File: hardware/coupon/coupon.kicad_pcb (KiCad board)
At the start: 4 copper layers, 100 x 80 mm, 78 parts, among them SW1 tactile

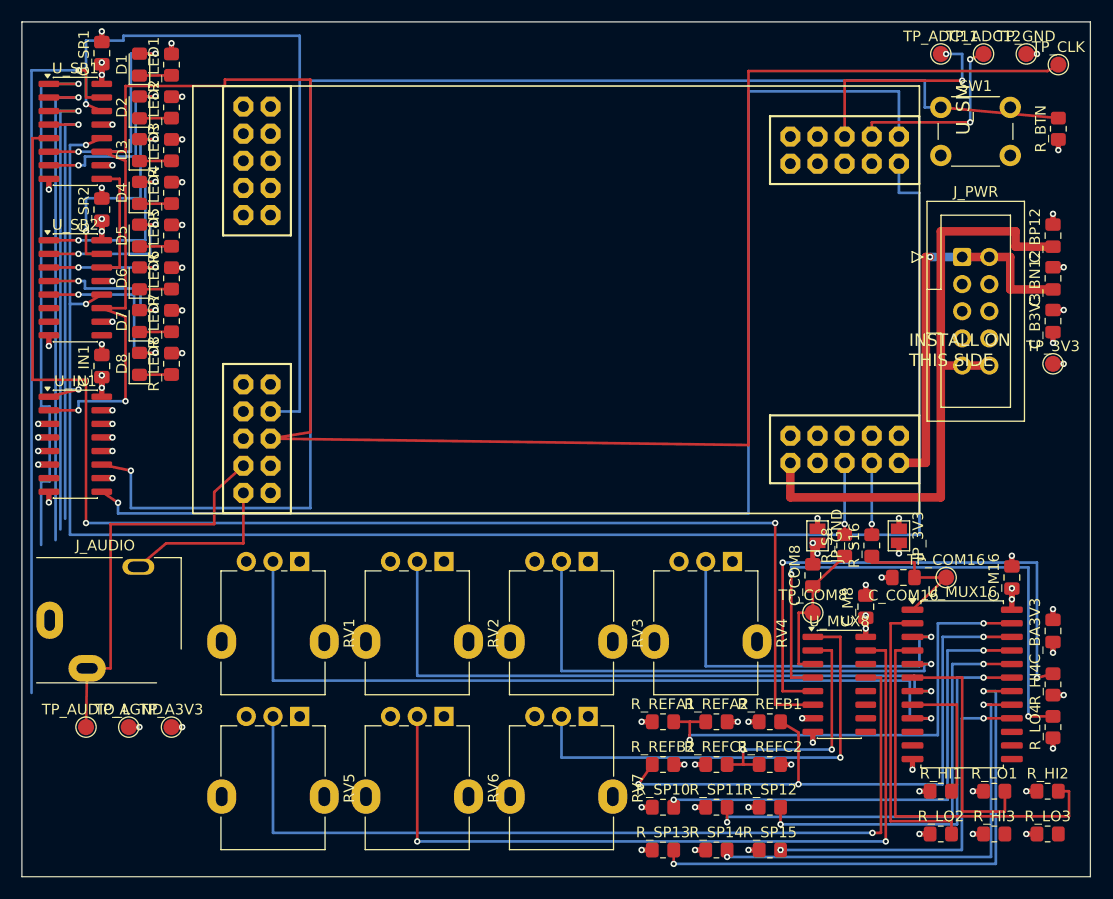
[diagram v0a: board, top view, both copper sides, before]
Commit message: hw(coupon): the tie comes to the mux, and the latch leaves the moat
Two controller rulings, both taken.

placement.py is data, so R_LO3 moved: (96, 76) -> (77.4, 69.6), 1.35 mm below
the 8:1's south edge and 6.3 mm from the pin it ties instead of 22. MUX8_CH3
is now a two-corner F.Cu drop through the package's own interior with no via,
and MUX8_CH1 -- unroutable last pass -- reaches R_HI3 down the strip between
the packages and along the board's southern edge, also without a via. Every
gate that depends on placement re-ran green, the stitcher re-derived its vias
around the moved part by itself, and the ratsnest went 11 -> 8.

R_HI3 stayed, and R_HI4/R_LO4 stayed, and both are decisions rather than
omissions -- the report has the arithmetic. The short version: the strip
between the two SOICs is 1.725 mm and carries four nets in four 0.45 mm
lanes, so a tie parked in it strands two of them; and the only slot within
5 mm of the 8:1's west-column pins is also the only F.Cu approach to its
enable, where a tie's stitching via lands 0.005 mm off the enable's lane.

SR_LATCH no longer runs the width of the board inside the plane gap. It sits
at y 47.4 now, inside the digital plane, which needed the two sense-drop vias
moved from y 47.0 to 46.2 -- at 47.0 there was no lane at all between
JP_GND's stitching via and the moat. Five moat crossings remain, all
perpendicular, none parallel to the gap.

Eight pairs are still open, all of them the address bus and the 16:1's enable
landing at the muxes. The corridor between the west edge and the muxes has
exactly one free 0.45 mm lane left and five nets want it; freeing the two
lanes MUX8_CH5/CH7 hold means bringing their ties to the package too, which
is a placement pass of its own.

Co-Authored-By: HAL 9000 <293417720+bea-ton-k@users.noreply.github.com>
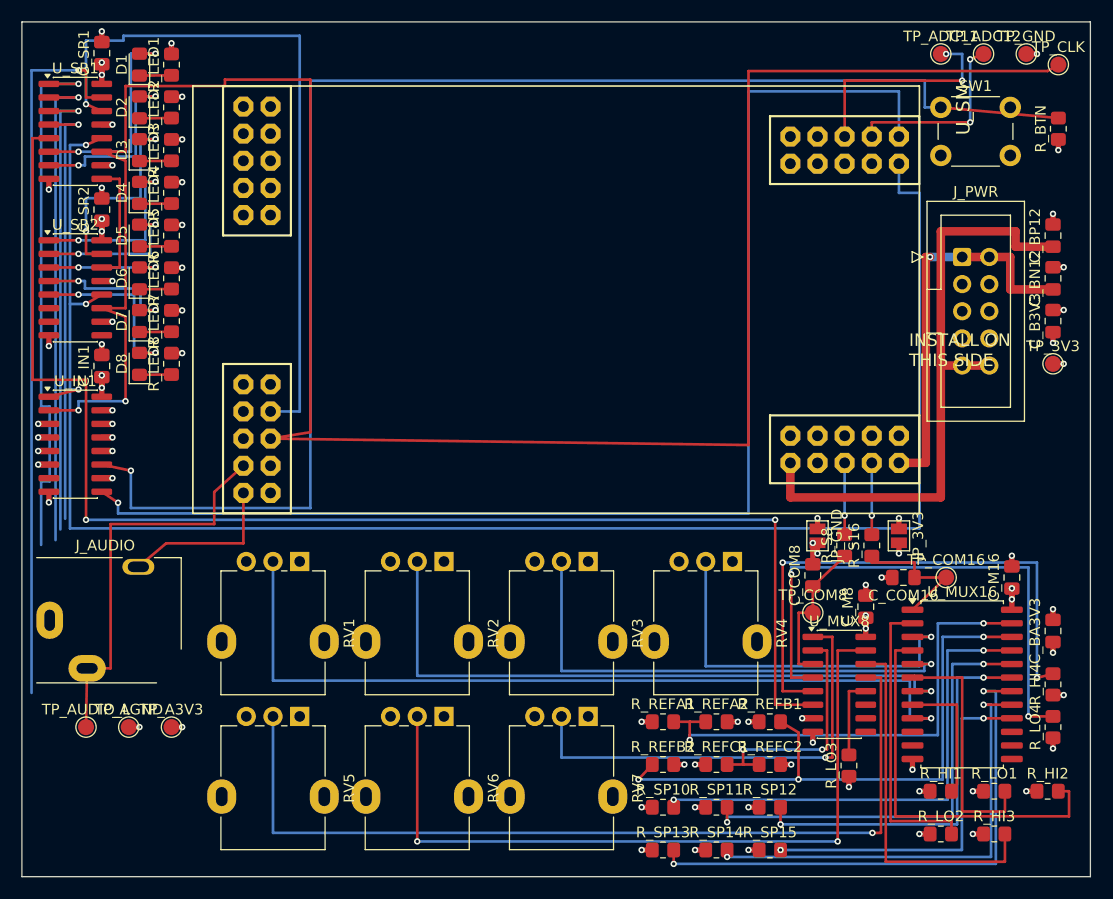
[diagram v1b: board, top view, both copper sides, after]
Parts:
- moved R_LO3 19.7 mm to (77.4, 69.6), turned to 90 degrees
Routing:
- net MUX8_CH1: track 0.00 -> 34.1 mm
- net MUX8_CH3: track 0.00 -> 7.54 mm
- net MUX8_CH2: track 75.3 -> 71.5 mm
- net MUX8_CH4: track 43.8 -> 42.3 mm
- net MUX16_CH9: track 57.8 -> 56.6 mm
- net SR_LATCH: track 162.6 -> 161.4 mm
- net MUX8_CH6: track 23.7 -> 22.8 mm

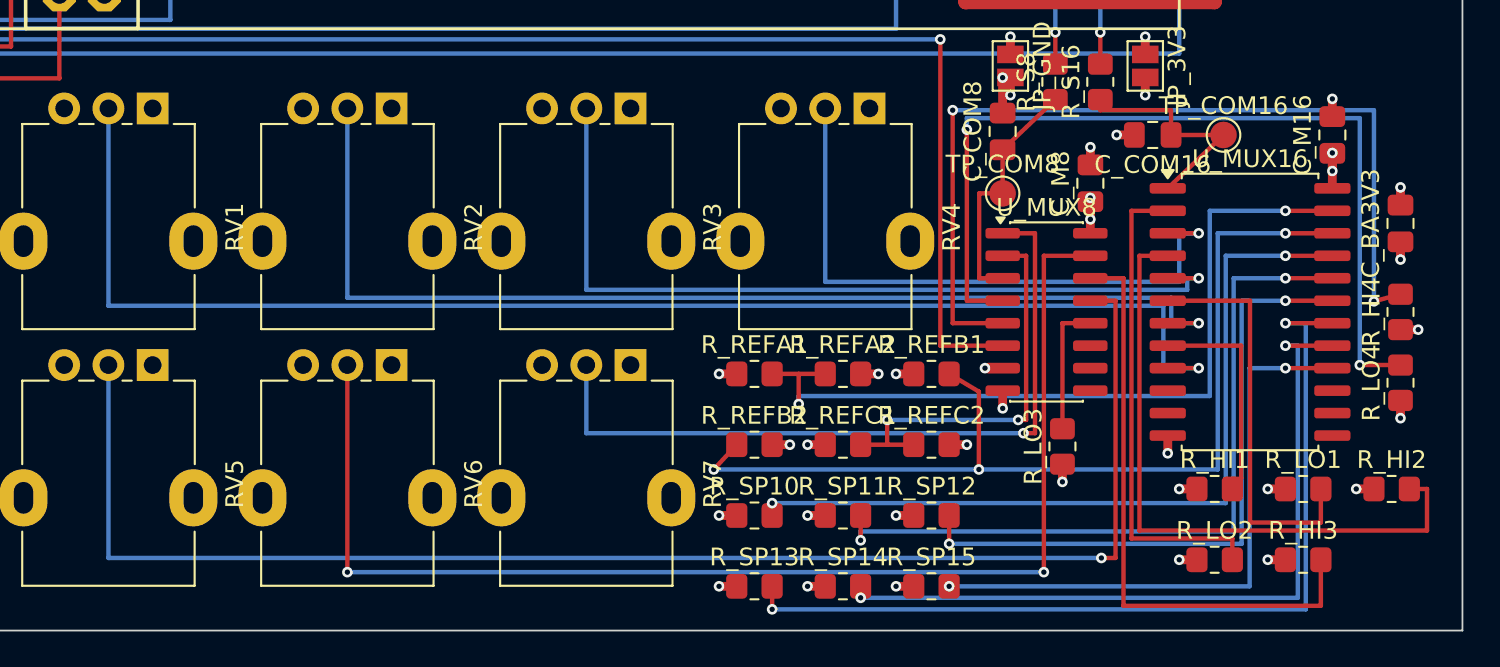
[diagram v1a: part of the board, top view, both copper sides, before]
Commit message: hw(coupon): WIP -- the interior takes the whole column, the strip empties
Placement pass 2, paused mid-flight. Steps 1-5 green; step 6 red with 3
tracks_crossing, all one cause -- MUX16_CH7's F.Cu vertical at x 86.0 cuts
the three stubs leaving the 16:1's west pad column at x 83.35 (CH5 at y
58.825, CH3 at 61.365, CH1 at 63.905). Step 7 red at 8 pairs: the address
bus and the 16:1's enable, unchanged.

What moved: R_LO3 to (78.4, 69.6) so the 8:1's interior can hold six 0.45 mm
lanes instead of five; MUX16_CH5 and CH7 out of the strip into the tie-row
gap; MUX8_CH0, CH1 and CH2 out of the strip into that interior. The strip
between the two packages is now empty, which is the point: MUX_A0 and MUX_A1
have to bridge the 8:1's east column and the 16:1's west column at y 63.905
and 65.175, and any full-height descent in that 2.375 mm strip cuts the
bridge.

R_LO4 went to the 8:1's west flank and came back. The finding is measured,
not assumed: its pads span x 70.9..72.3, which is where MUX8_CH5's only west
exit runs, and the corridor left between those pads and MUX8_COM's fixed
vertical at x 72.7 is 0.4 mm against the 0.65 mm a 0.25 mm track needs. The
interior cannot absorb CH5 either -- its six lanes are the 8:1's whole right
column plus the two left-column channels that MUX8_COM blocks from leaving
west.

Co-Authored-By: HAL 9000 <293417720+bea-ton-k@users.noreply.github.com>
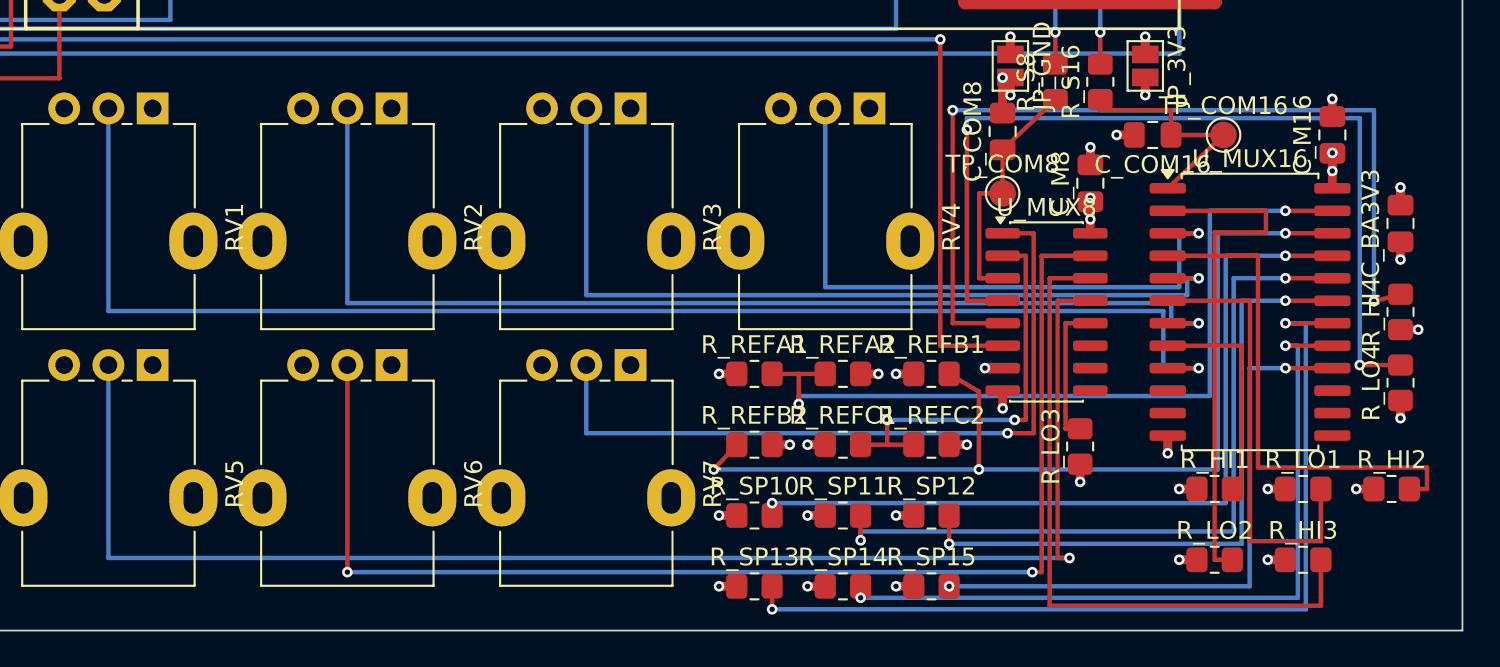
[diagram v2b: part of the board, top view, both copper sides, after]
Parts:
- moved R_LO3 1.00 mm to (78.4, 69.6)
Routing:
- net MUX16_CH5: track 36.7 -> 28.8 mm
- net MUX8_CH1: track 34.1 -> 38.7 mm
- net MUX16_CH3: track 23.1 -> 25.2 mm
- net MUX16_CH7: track 27.5 -> 29.2 mm
- net MUX8_CH0: track 83.8 -> 82.3 mm
- net MUX8_CH3: track 7.54 -> 8.19 mm
- net MUX16_CH6: track 35.4 -> 36.0 mm
- net MUX16_CH4: track 47.3 -> 47.9 mm

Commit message: hw(coupon): the SMD pads were never walls, and the last net lands
The pause left one crossing and eight unconnected pairs, and the intended
fix -- a descent east of the west-column stubs -- turns out not to exist:
the only lane there sits west of CH5's stub end, and any descent that does
clear it is then crossed by CH3's own leg to R_LO1. CH7 goes west into the
strip instead and comes back between the tie rows. No via, no crossing.

The address bus moved on one measurement: every mux, cap, resistor and
test-point pad on this board is SMD, so it blocks F.Cu only. B.Cu runs
under both SOICs, under both tie rows and under every 0805, and what
actually walls the analog half off is Task 3's stitching, the pots' and the
jack's through-holes, and this task's own earlier lanes. Three corridors
fall out of that: the y-62 band under the 8:1, the F.Cu band between the
upper pots' pins and their lugs, and the single lane that threads C_M8's
and C_M16's vias at y 54.75. A0/A1/A2 take the first, A3 and EN16 the
second and third, and all five reach the 16:1's east column through the
2.1 mm pocket east of the package -- the interior is closed by eight via
stubs and six descents, enumerated, not assumed.

CH8 and MUX8_CH1 gave up a lane each so the strip bridges and the south
runs have somewhere to be. Nothing in placement.py moved.

Seven of seven green: 168 tracks, 368 segments, 88 signal vias, zero
crossings, ratsnest zero on both counters. Step 7 was proved red once by
deleting EN16's last stub; steps 1-6 stayed green and both counters moved
together.

The bus still crosses the moat at the west edge rather than beside the star
point, and the reason is measured: CH5's and CH7's lanes at y 50.6/51.05
leave exactly one descent between the moat and the muxes. The report names
the placement change that would open three.

Co-Authored-By: HAL 9000 <293417720+bea-ton-k@users.noreply.github.com>
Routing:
- net MUX_A2: track 46.4 -> 183.2 mm, vias 1 -> 4
- net MUX_A3: track 43.6 -> 174.8 mm, vias 1 -> 6
- net MUX16_EN_N: track 40.9 -> 152.2 mm, vias 1 -> 4
- net MUX_A1: track 51.0 -> 156.5 mm, vias 1 -> 5
- net MUX_A0: track 67.4 -> 158.6 mm, vias 1 -> 3
- net MUX16_CH8: track 45.8 -> 49.0 mm
- net MUX16_CH7: track 29.2 -> 26.3 mm
- net MUX8_CH1: track 38.7 -> 39.5 mm, vias 0 -> 2

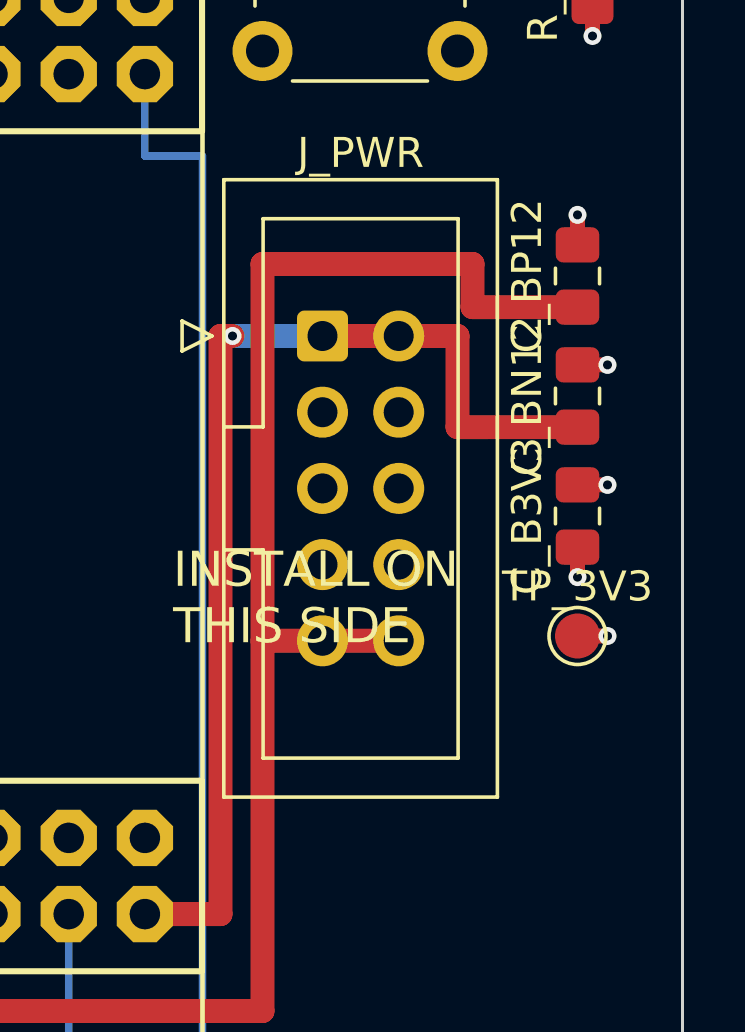
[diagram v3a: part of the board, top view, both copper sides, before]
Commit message: hw(coupon): five rules become a checker, and one bulk cap moves to answer it
check_layout.py measures the plan's five gated analog rules plus the
spec's ungated 0R tie distances (Ruling A), against the saved board --
never asserted. Two checker bugs found and fixed along the way: audio
clearance needs a real Liang-Barsky clip at the SM footprint boundary,
not a whole-segment skip, or an SM pad's own inside-shadow endpoint
dominates the measurement; and the decoupler rule needs the VCC pin
NUMBER resolved through the same symbol lookup netlist.py used to build
the board, because 74HC595's SRCLR~ is tied to +3V3 right next to the
real VCC pin and a net-based pad search can silently grab the wrong one.

One real placement gap surfaced: C_BP12 measured 12.62 mm from its
nearest +12V pad, stacked at the wrong end of the IDC header's row order.
It moves 16 mm down its own column to 7.70 mm, and +-12V's track picks a
new path around the whole bulk-cap column rather than through the narrow
gap DRC flagged as a real tracks_crossing. Build proof runs eight steps
green; --sabotage decoupling proves the checker can still go red.

Co-Authored-By: HAL 9000 <293417720+bea-ton-k@users.noreply.github.com>
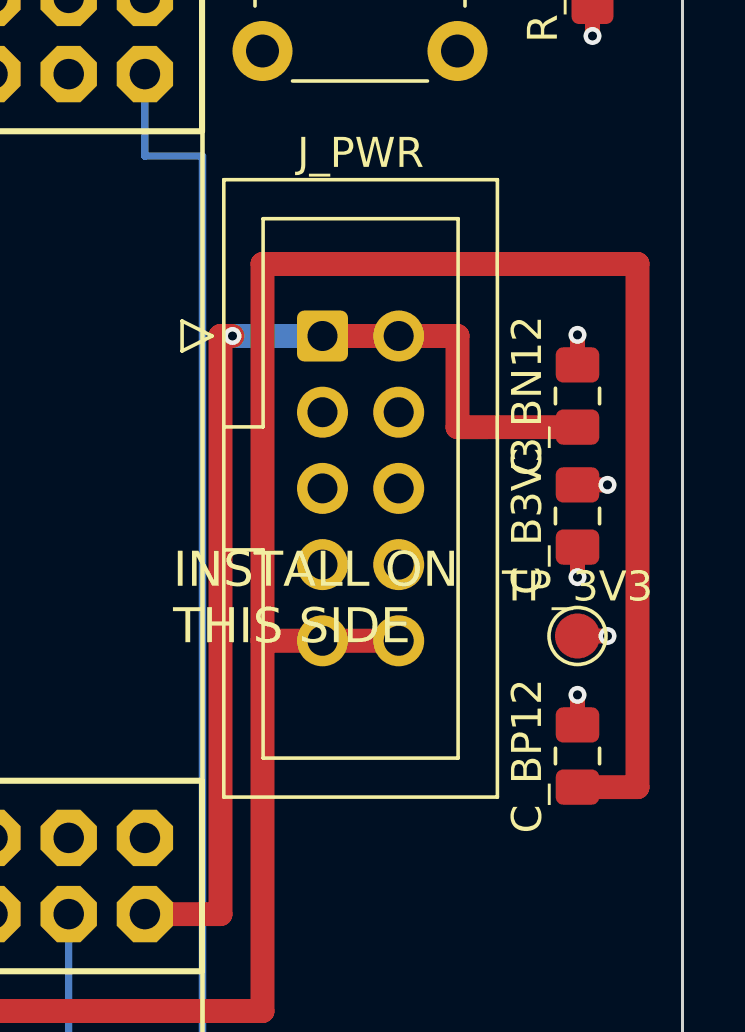
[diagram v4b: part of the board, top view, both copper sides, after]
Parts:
- moved C_BP12 16.0 mm to (96.5, 36.0)
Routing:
- net +12V: track 58.7 -> 78.7 mm
